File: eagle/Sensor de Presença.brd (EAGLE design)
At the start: 100 x 80 mm, 4 parts

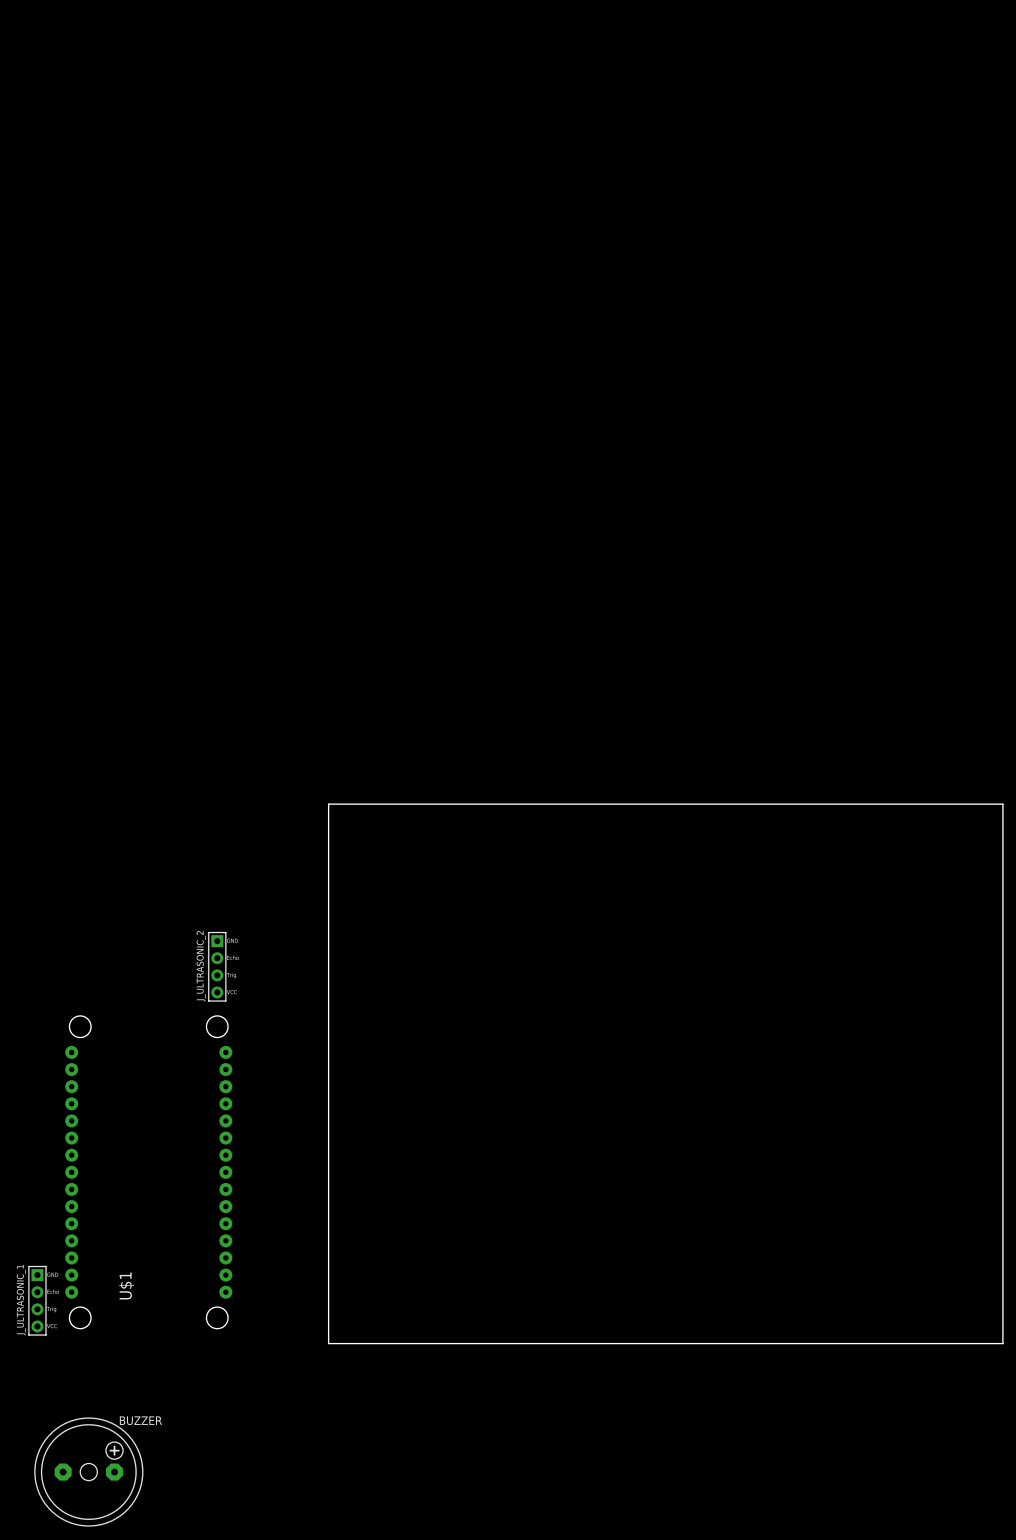
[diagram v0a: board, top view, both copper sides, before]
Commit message: updated eagle project to include 2 ultrassonic sensors and ds1307 rtc
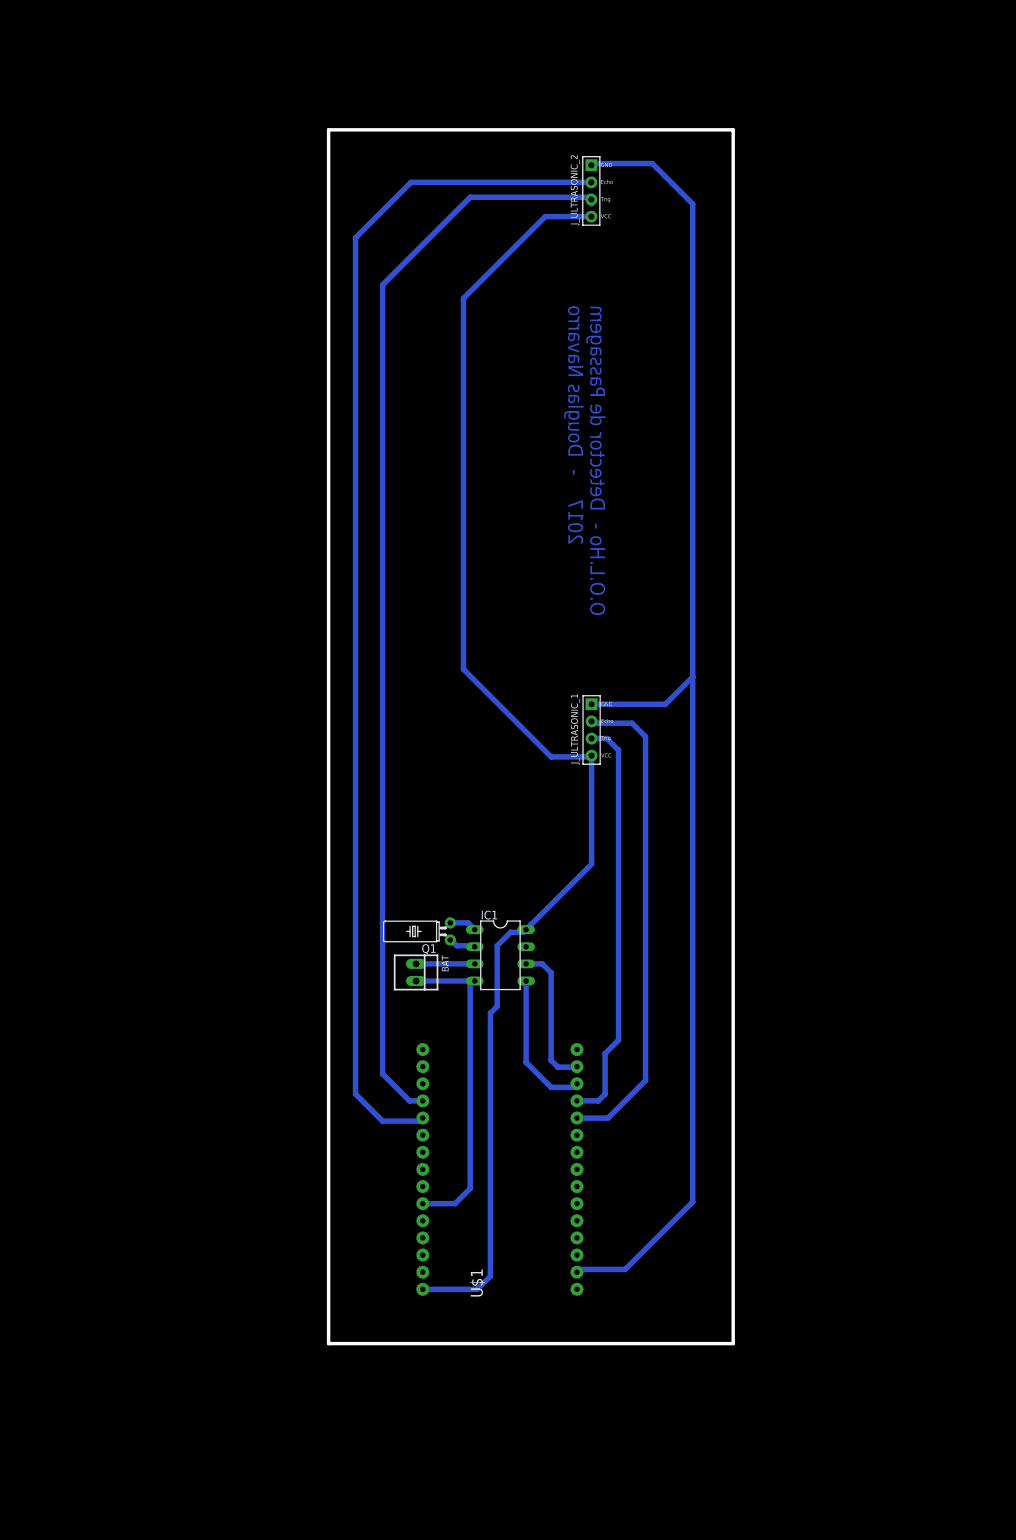
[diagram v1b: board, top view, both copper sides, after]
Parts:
- removed BUZZER: F/HMB, buzzer:F/HMB
- added BAT: 22-23-2021, con-molex:22-23-2021
- added IC1: DS1307, adafruit:DIL08
- added Q1: (no value), adafruit:TC38H
- moved J_ULTRASONIC_2 127.7 mm to (39.0, 170.9)
- moved J_ULTRASONIC_1 118.0 mm to (39.0, 91.0)
- moved U$1 52.1 mm to (25.4, 25.8)
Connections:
- removed net BUZZ_SIG: BUZZER.+
- new net N$1: IC1.1, Q1.2
- new net N$2: IC1.2, Q1.1
- new net SCL: IC1.6, U$1.D1
- new net SDA: IC1.5, U$1.D2
- new net VBAT: BAT.1, IC1.3
- net ECHO1: now also U$1.D4; no longer U$1.D2
- net ECHO2: now also U$1.SD2; no longer U$1.D5
- net GND: now also BAT.2, IC1.4, U$1.GND@0, U$1.GND@1, U$1.GND@2; no longer BUZZER.-
- net TRIG2: now also U$1.SD3; no longer U$1.D6
- net VCC: now also IC1.8
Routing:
- net GND: track 0.00 -> 253.6 mm
- net VCC: track 0.00 -> 200.0 mm
- net ECHO2: track 0.00 -> 177.2 mm
- net TRIG2: track 0.00 -> 161.8 mm
- net ECHO1: track 0.00 -> 72.4 mm
- net TRIG1: track 0.00 -> 61.1 mm
- net SCL: track 0.00 -> 21.5 mm
- net SDA: track 0.00 -> 21.4 mm
- net VBAT: track 0.00 -> 8.70 mm
- net N$1: track 0.00 -> 4.03 mm
- net N$2: track 0.00 -> 4.03 mm
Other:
- board size 100 x 80 mm -> 60 x 180 mm
- board text added: "O.O.L.Ho - Detector de Passagem 2017 - Douglas Navarro"

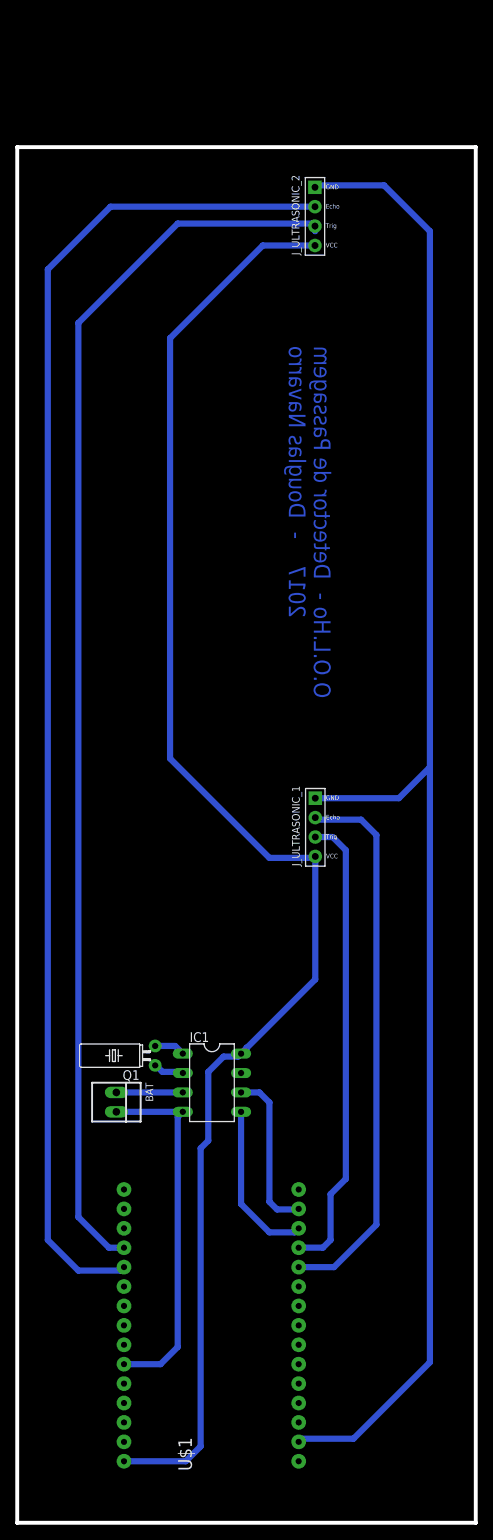
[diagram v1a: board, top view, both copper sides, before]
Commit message: added final prototype pcb layout and text
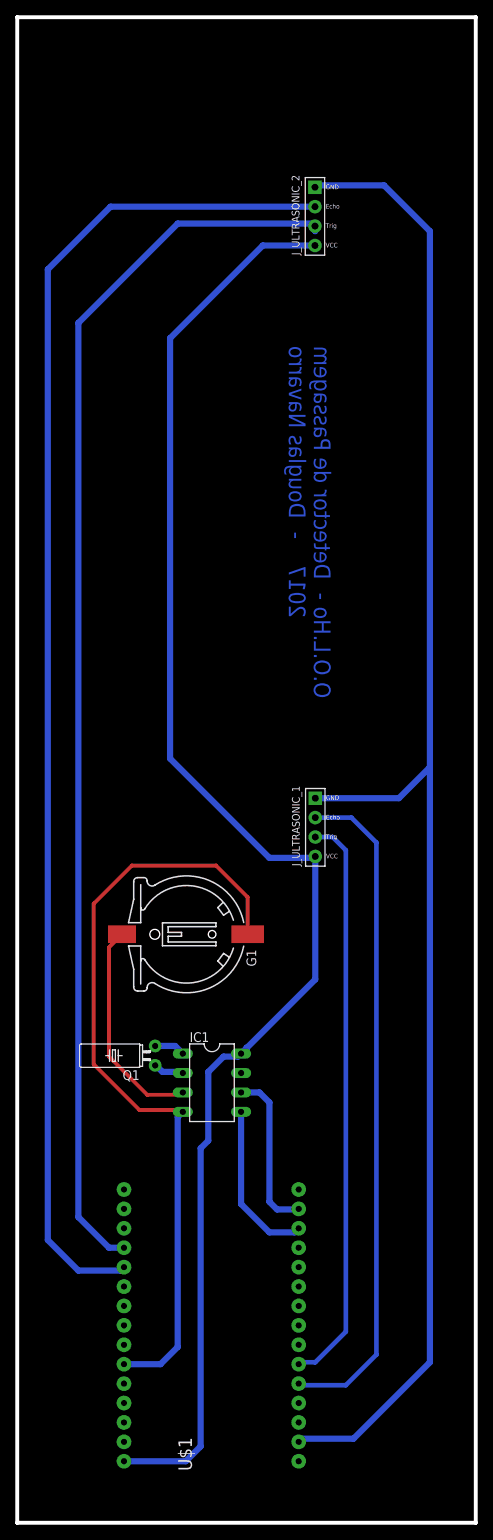
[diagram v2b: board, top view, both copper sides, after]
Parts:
- removed BAT: 22-23-2021, con-molex:22-23-2021
- added G1: CH291-1220LF, battery:CH291-1220LF
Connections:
- net ECHO1: now also U$1.D8; no longer U$1.D4
- net GND: now also G1.-; no longer BAT.2
- net TRIG1: now also U$1.D7; no longer U$1.D3
- net VBAT: now also G1.+; no longer BAT.1
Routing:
- net GND: track 253.6 -> 306.8 mm
- net VBAT: track 8.70 -> 28.6 mm
- net ECHO1: track 72.4 -> 88.3 mm
- net TRIG1: track 61.1 -> 75.6 mm
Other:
- board size 60 x 180 mm -> 60 x 197 mm
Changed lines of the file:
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@@
 <board>
 <plain>
-<wire x1="0" y1="0" x2="0" y2="180" width="0.508" layer="20"/>
+<wire x1="0" y1="0" x2="0" y2="197" width="0.508" layer="20"/>
 <wire x1="0" y1="0" x2="60" y2="0" width="0.508" layer="20"/>
-<wire x1="60" y1="180" x2="0" y2="180" width="0.508" layer="20"/>
-<wire x1="60" y1="0" x2="60" y2="180" width="0.508" layer="20"/>
+<wire x1="60" y1="0" x2="60" y2="197" width="0.508" layer="20"/>
 <text x="41" y="154" size="2.1844" layer="16" rot="MR270">O.O.L.Ho -  Detector de Passagem
     2017    -  Douglas Navarro
 </text>
+<wire x1="0" y1="197" x2="60" y2="197" width="0.508" layer="20"/>
 </plain>
 <attributes>
@@
 <element name="U$1" library="ESP12E_DEVKIT" package="ESP12E_DEVKIT" value="ESP12E_DEVKIT" x="25.4" y="25.83"/>
 <element name="IC1" library="adafruit" library_urn="urn:adsk.eagle:library:420" package="DIL08" value="DS1307" x="25.48" y="57.58" rot="R270"/>
-<element name="BAT" library="con-molex" library_urn="urn:adsk.eagle:library:165" package="22-23-2021" value="22-23-2021" x="12.97" y="55.04" rot="R270">
-<attribute name="MF" value="MOLEX" x="12.97" y="55.04" size="1.778" layer="27" rot="R270" display="off"/>
-<attribute name="MPN" value="22-23-2021" x="12.97" y="55.04" size="1.778" layer="27" rot="R270" display="off"/>
-<attribute name="OC_FARNELL" value="1462926" x="12.97" y="55.04" size="1.778" layer="27" rot="R270" display="off"/>
-<attribute name="OC_NEWARK" value="25C3832" x="12.97" y="55.04" size="1.778" layer="27" rot="R270" display="off"/>
-</element>
 <element name="Q1" library="adafruit" library_urn="urn:adsk.eagle:library:420" package="TC38H" value="" x="18.05" y="61.12" rot="R90">
 <attribute name="MF" value="" x="18.05" y="61.12" size="1.778" layer="27" rot="R90" display="off"/>
@@
 <attribute name="OC_NEWARK" value="unknown" x="18.05" y="61.12" size="1.778" layer="27" rot="R90" display="off"/>
 </element>
+<element name="G1" library="battery" library_urn="urn:adsk.eagle:library:109" package="CH291-1220LF" value="CH291-1220LF" x="16" y="77" rot="R270"/>
 </elements>
 <signals>
@@
 <contactref element="U$1" pad="GND@3"/>
 <contactref element="IC1" pad="4"/>
-<contactref element="BAT" pad="2"/>
 <contactref element="U$1" pad="GND@1"/>
 <contactref element="U$1" pad="GND@0"/>
 <contactref element="U$1" pad="GND@2"/>
-<wire x1="21.67" y1="53.77" x2="12.97" y2="53.77" width="0.8128" layer="16"/>
-<wire x1="12.23" y1="53.77" x2="12.97" y2="53.77" width="0.8128" layer="16"/>
-<wire x1="12" y1="54" x2="12.23" y2="53.77" width="0.8128" layer="16"/>
-<wire x1="12" y1="54" x2="12.74" y2="54" width="0.8128" layer="16"/>
-<wire x1="12.74" y1="54" x2="12.97" y2="53.77" width="0.8128" layer="16"/>
 <wire x1="13.97" y1="20.75" x2="18.75" y2="20.75" width="0.8128" layer="16"/>
 <wire x1="18.75" y1="20.75" x2="21" y2="23" width="0.8128" layer="16"/>
@@
 <wire x1="39" y1="94.81" x2="49.941790625" y2="94.81" width="0.8128" layer="16"/>
 <wire x1="49.941790625" y1="94.81" x2="54" y2="98.868209375" width="0.8128" layer="16"/>
+<contactref element="G1" pad="-"/>
+<wire x1="30.1458" y1="77" x2="30.1458" y2="81.8542" width="0.508" layer="1"/>
+<wire x1="30.1458" y1="81.8542" x2="26" y2="86" width="0.508" layer="1"/>
+<wire x1="26" y1="86" x2="15" y2="86" width="0.508" layer="1"/>
+<wire x1="15" y1="86" x2="10" y2="81" width="0.508" layer="1"/>
+<wire x1="10" y1="81" x2="10" y2="60" width="0.508" layer="1"/>
+<wire x1="10" y1="60" x2="16" y2="54" width="0.508" layer="1"/>
+<wire x1="16" y1="54" x2="21.44" y2="54" width="0.508" layer="1"/>
+<wire x1="21.44" y1="54" x2="21.67" y2="53.77" width="0.508" layer="1"/>
 <wire x1="21" y1="23" x2="36.83" y2="28.37" width="0" layer="19" extent="16-16"/>
 <wire x1="13.97" y1="10.59" x2="13.97" y2="20.75" width="0" layer="19" extent="1-1"/>
-<wire x1="37.24" y1="11" x2="36.83" y2="28.37" width="0" layer="19" extent="16-16"/>
+<wire x1="39" y1="94.81" x2="30.1458" y2="81.8542" width="0" layer="19" extent="1-1"/>
 </signal>
 <signal name="ECHO1">
 <contactref element="J_ULTRASONIC_1" pad="ECHO"/>
-<contactref element="U$1" pad="D4"/>
-<wire x1="39" y1="92.27" x2="39.27" y2="92" width="0.8128" layer="16"/>
-<wire x1="39.27" y1="92" x2="45" y2="92" width="0.8128" layer="16"/>
-<wire x1="45" y1="92" x2="47" y2="90" width="0.8128" layer="16"/>
-<wire x1="47" y1="90" x2="47" y2="39" width="0.8128" layer="16"/>
-<wire x1="47" y1="39" x2="41.45" y2="33.45" width="0.8128" layer="16"/>
-<wire x1="41.45" y1="33.45" x2="36.83" y2="33.45" width="0.8128" layer="16"/>
+<contactref element="U$1" pad="D8"/>
+<wire x1="39" y1="92.27" x2="43.73" y2="92.27" width="0.6096" layer="16"/>
+<wire x1="43.73" y1="92.27" x2="47" y2="89" width="0.6096" layer="16"/>
+<wire x1="47" y1="89" x2="47" y2="22" width="0.6096" layer="16"/>
+<wire x1="47" y1="22" x2="43" y2="18" width="0.6096" layer="16"/>
+<wire x1="43" y1="18" x2="37.04" y2="18" width="0.6096" layer="16"/>
+<wire x1="37.04" y1="18" x2="36.83" y2="18.21" width="0.6096" layer="16"/>
 </signal>
 <signal name="TRIG1">
 <contactref element="J_ULTRASONIC_1" pad="TRIG"/>
-<contactref element="U$1" pad="D3"/>
-<wire x1="36.83" y1="35.99" x2="36.84" y2="36" width="0.8128" layer="16"/>
-<wire x1="36.84" y1="36" x2="40" y2="36" width="0.8128" layer="16"/>
-<wire x1="40" y1="36" x2="41" y2="37" width="0.8128" layer="16"/>
-<wire x1="41" y1="37" x2="41" y2="43" width="0.8128" layer="16"/>
-<wire x1="41" y1="43" x2="43" y2="45" width="0.8128" layer="16"/>
-<wire x1="43" y1="45" x2="43" y2="88" width="0.8128" layer="16"/>
-<wire x1="43" y1="88" x2="41.27" y2="89.73" width="0.8128" layer="16"/>
-<wire x1="41.27" y1="89.73" x2="39" y2="89.73" width="0.8128" layer="16"/>
+<contactref element="U$1" pad="D7"/>
+<wire x1="39" y1="89.73" x2="41.27" y2="89.73" width="0.6096" layer="16"/>
+<wire x1="41.27" y1="89.73" x2="43" y2="88" width="0.6096" layer="16"/>
+<wire x1="43" y1="88" x2="43" y2="25" width="0.6096" layer="16"/>
+<wire x1="43" y1="25" x2="39" y2="21" width="0.6096" layer="16"/>
+<wire x1="39" y1="21" x2="37.08" y2="21" width="0.6096" layer="16"/>
+<wire x1="37.08" y1="21" x2="36.83" y2="20.75" width="0.6096" layer="16"/>
 </signal>
 <signal name="ECHO2">
@@
 <wire x1="38.63" y1="170" x2="38.96" y2="169.67" width="0.8128" layer="16"/>
 </signal>
-<signal name="VBAT">
-<contactref element="BAT" pad="1"/>
-<contactref element="IC1" pad="3"/>
-<wire x1="12.97" y1="56.31" x2="21.67" y2="56.31" width="0.8128" layer="16"/>
-</signal>
 <signal name="SCL">
 <contactref element="IC1" pad="6"/>
@@
 <wire x1="21.52" y1="59" x2="21.67" y2="58.85" width="0.8128" layer="16"/>
 </signal>
+<signal name="VBAT">
+<contactref element="IC1" pad="3"/>
+<contactref element="G1" pad="+"/>
+<wire x1="13.7045" y1="77" x2="12" y2="75.2955" width="0.508" layer="1"/>
+<wire x1="12" y1="75.2955" x2="12" y2="61" width="0.508" layer="1"/>
+<wire x1="12" y1="61" x2="17" y2="56" width="0.508" layer="1"/>
+<wire x1="17" y1="56" x2="21.36" y2="56" width="0.508" layer="1"/>
+<wire x1="21.36" y1="56" x2="21.67" y2="56.31" width="0.508" layer="1"/>
+</signal>
 </signals>
